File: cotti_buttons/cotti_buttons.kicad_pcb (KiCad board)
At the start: 2 copper layers, 50.8 x 20.3 mm, 26 parts, among them J1 Pmod GPIO 1x06 pin, SW1 SW_Push_Dual, SW2 SW_Push_Dual, SW3 SW_Push_Dual, SW4 SW_Push_Dual, U1 Invert Schmitt, U2 Invert Schmitt, U3 Invert Schmitt, U4 Invert Schmitt

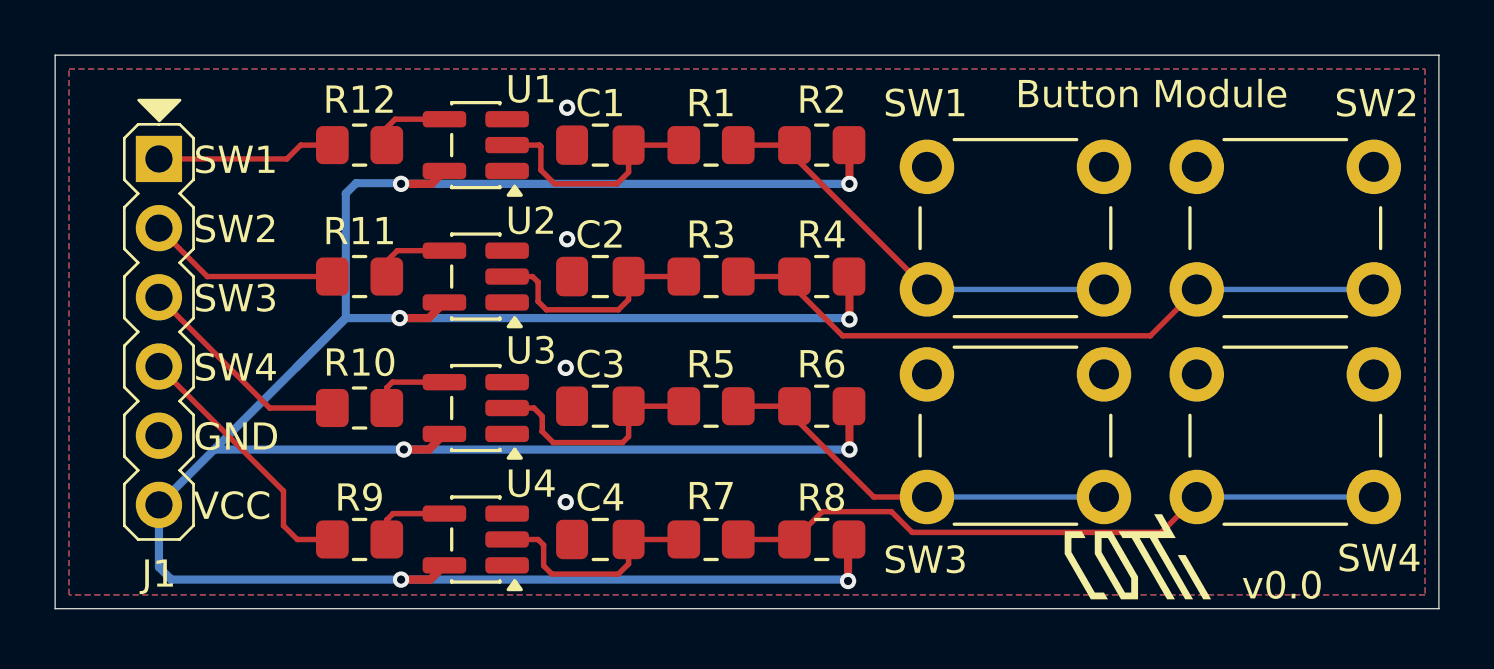
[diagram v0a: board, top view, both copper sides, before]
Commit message: feat: cotti uttons with new libs
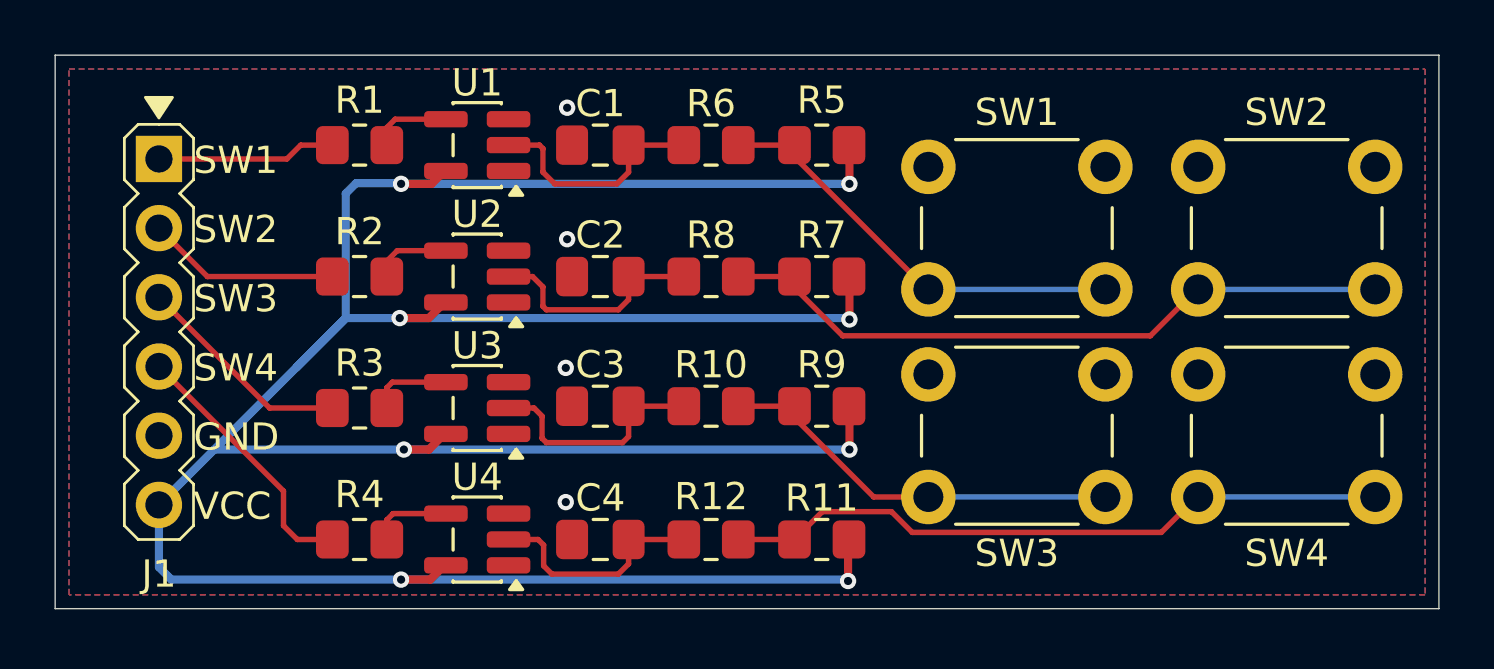
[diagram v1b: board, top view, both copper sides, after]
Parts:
- removed the R10 at (138.2, 114.6)
- removed the R11 at (138.2, 109.7)
- removed the R12 at (138.2, 104.9)
- removed the R9 at (138.2, 119.4)
- removed the REF** at (164.1, 119.1)
- added R1: 200R, Resistor_SMD:R_0805_2012Metric_Pad1.20x1.40mm_HandSolder, F.Cu at (138.2, 104.9)
- added R2: 200R, Resistor_SMD:R_0805_2012Metric_Pad1.20x1.40mm_HandSolder, F.Cu at (138.2, 109.7)
- added R3: 200R, Resistor_SMD:R_0805_2012Metric_Pad1.20x1.40mm_HandSolder, F.Cu at (138.2, 114.6)
- added R4: 200R, Resistor_SMD:R_0805_2012Metric_Pad1.20x1.40mm_HandSolder, F.Cu at (138.2, 119.4)
- added REF**: cotti_logo_filled H=7.5mm T=0.75mm, cotti_logo:cotti_logo_filled H=7.5mm T=0.75mm, B.Cu at (153.0, 109.5)
- J1: footprint Pmod:Pmod_1x06_pin -> cotti_footprints:Pmod_1x06_pin
- U1, U2, U3, U4: value Invert Schmitt -> MC74VHC1GT14DBVT1G
- moved SW1 0.05 mm to (159.1, 105.7)
- moved SW3 0.05 mm to (159.1, 113.3)
- moved SW2 0.05 mm to (169.0, 105.7)
- moved SW4 0.05 mm to (169.0, 113.3)
- moved U1 0.05 mm to (142.5, 104.9)
- moved U2 0.05 mm to (142.5, 109.7)
- moved U3 0.05 mm to (142.5, 114.6)
- moved U4 0.05 mm to (142.5, 119.4)
- renumbered R5 to R10, R8 to R11, R7 to R12, R2 to R5, R1 to R6, R4 to R7, R3 to R8, R6 to R9
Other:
- board text added: "Rev 0.0"
- board text removed: "v0.0"
